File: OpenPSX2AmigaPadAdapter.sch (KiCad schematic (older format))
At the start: 46 parts, among them J1 TO_PSX_PAD, J2 DB9_F, J3 CONN_FTDI, J4 CONN_ICSP, J99 OSHW_LOGO, Q1 BSS138, Q2 BSS138, Q3 BSS138, Q4 BSS138, Q5 BSS138, U1 ATmega328P-AU, U2 TC1185-3.3V, U3 AD5242, Y1 16M, Y2 16M

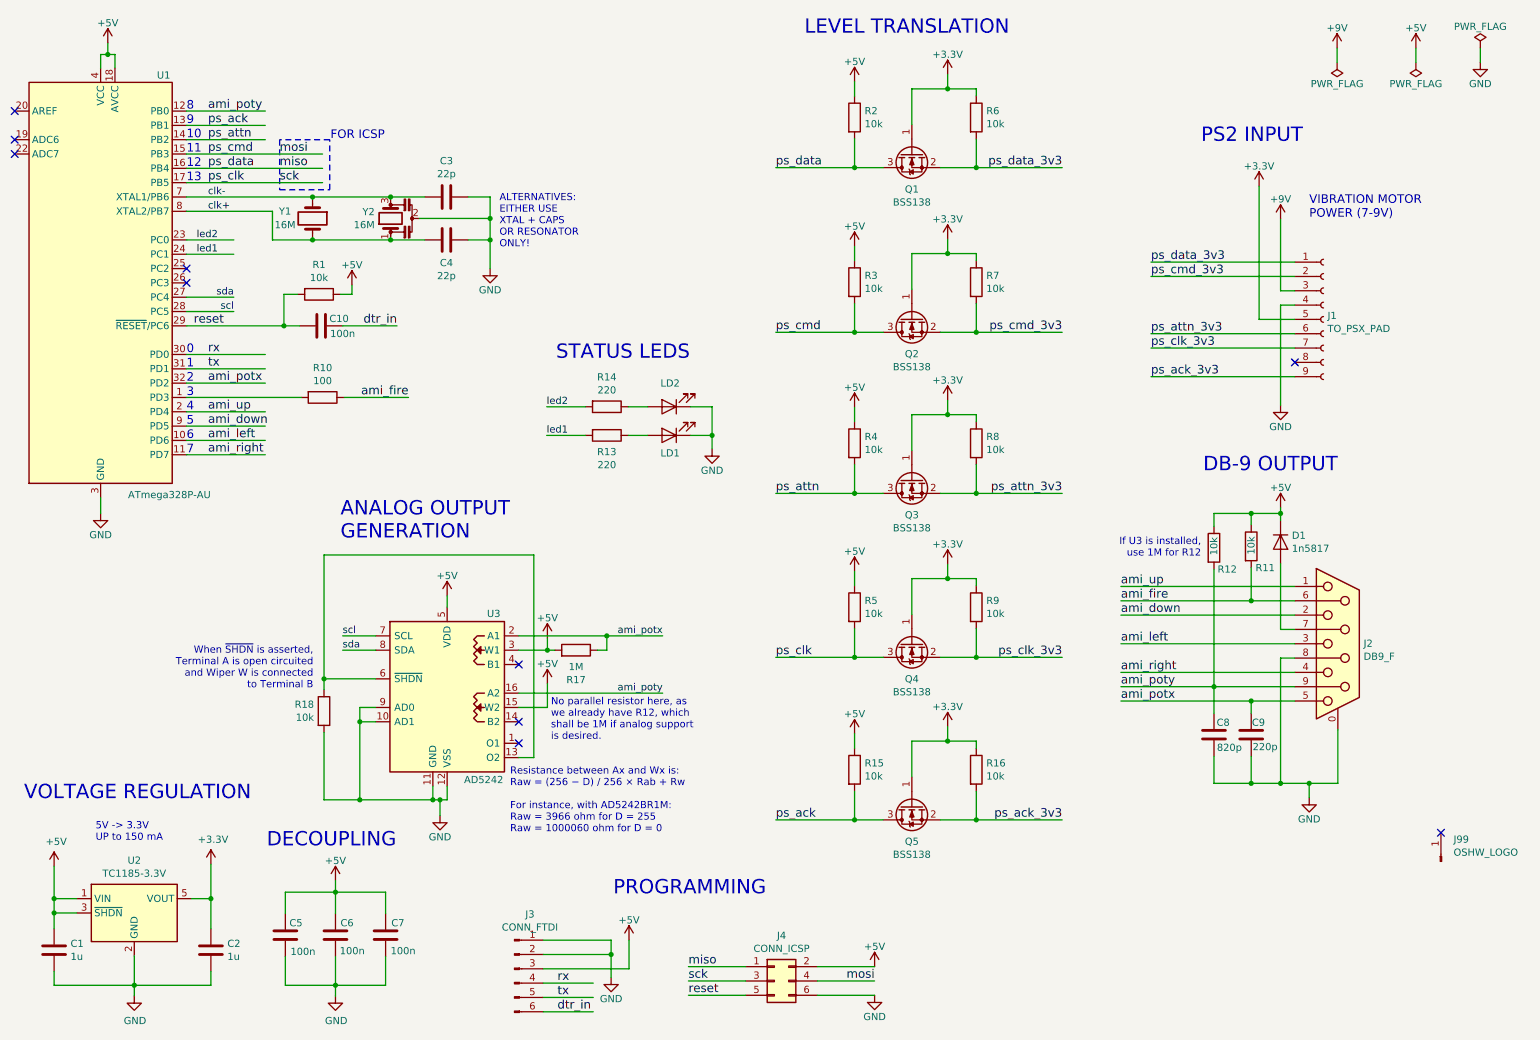
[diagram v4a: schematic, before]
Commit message: Make schematics clearer
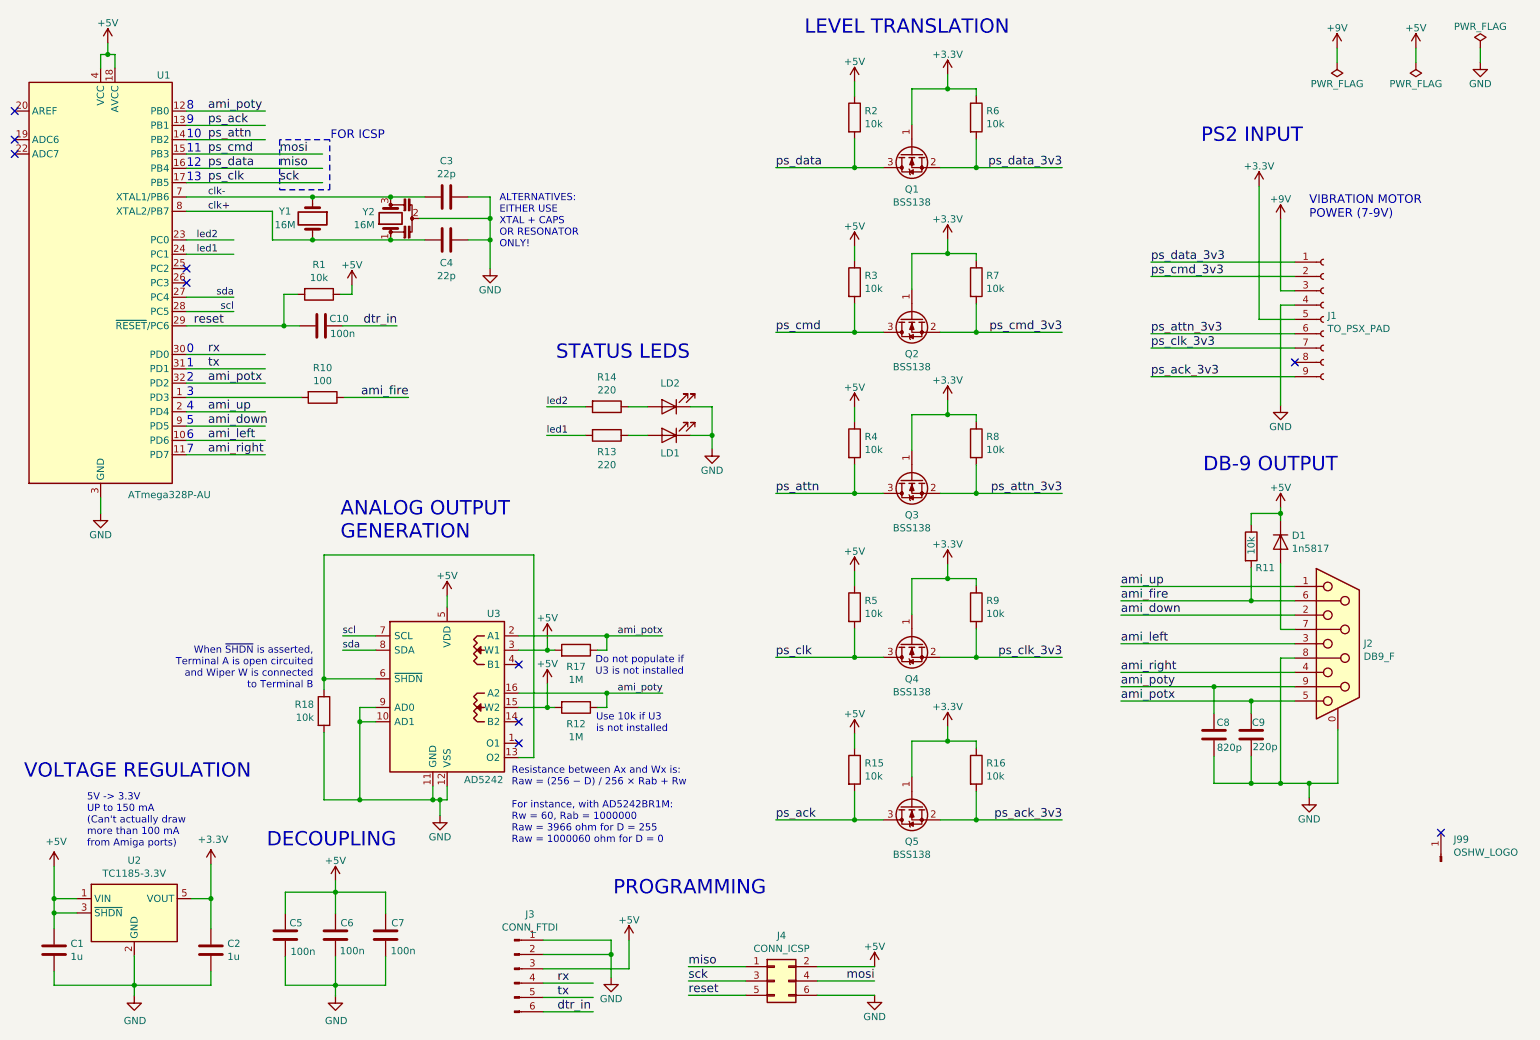
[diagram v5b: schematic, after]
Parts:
- R12: value 10k -> 1M
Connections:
- wire segments 232 -> 233
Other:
- note added: "5V -> 3.3V\nUP to 150 mA\n(Can't actually draw\nmore than 100 mA\nfrom Amiga ports)"
- note added: "Do not populate if\nU3 is not installed"
- note added: "Resistance between Ax and Wx is:\nRaw = (256 − D) / 256 × Rab + Rw\n\nFor instance, with AD5242BR1M:\nRw = 60, Rab = 1000000\nRaw = 3966 ohm for D = 255\nRaw = 1000060 ohm for D = 0"
- note added: "Use 10k if U3\nis not installed"
- note removed: "5V -> 3.3V\nUP to 150 mA"
- note removed: "If U3 is installed,\nuse 1M for R12"
- note removed: "No parallel resistor here, as\nwe already have R12, which\nshall be 1M if analog support\nis desired."
- note removed: "Resistance between Ax and Wx is:\nRaw = (256 − D) / 256 × Rab + Rw\n\nFor instance, with AD5242BR1M:\nRaw = 3966 ohm for D = 255\nRaw = 1000060 ohm for D = 0"
- moved on the sheet: R12
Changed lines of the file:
@@
 	9505 4050 9505 4010
-Wire Wire Line
-	9040 4140 9040 4050
-Wire Wire Line
-	9040 4050 9300 4050
-Connection ~ 9300 4050
 Wire Wire Line
 	9300 4430 9300 4660
@@
 Wire Wire Line
 	9300 4660 8390 4660
-Wire Wire Line
-	9040 4440 9040 5260
 Connection ~ 9040 5260
 Wire Wire Line
@@
 L Device:R R12
 U 1 1 5DAFD7E8
-P 9040 4290
-F 0 "R12" H 9200 4140 50  0000 R CNN
-F 1 "10k" V 9040 4365 50  0000 R CNN
-F 2 "Resistor_SMD:R_0805_2012Metric_Pad1.15x1.40mm_HandSolder" V 8970 4290 50  0001 C CNN
-F 3 "~" H 9040 4290 50  0001 C CNN
-	1    9040 4290
-	1    0    0    -1
+P 4585 5405
+F 0 "R12" V 4700 5405 50  0000 C CNN
+F 1 "1M" V 4791 5405 50  0000 C CNN
+F 2 "Resistor_SMD:R_0805_2012Metric_Pad1.15x1.40mm_HandSolder" V 4515 5405 50  0001 C CNN
+F 3 "~" H 4585 5405 50  0001 C CNN
+	1    4585 5405
+	0    1    1    0
 $EndComp
 $Comp
@@
 AR Path="/5EFED7F9/5F065454" Ref="R?"  Part="1"
 AR Path="/5F065454" Ref="R17"  Part="1"
-F 0 "R17" V 4378 5005 50  0000 C CNN
-F 1 "1M" V 4469 5005 50  0000 C CNN
+F 0 "R17" V 4470 5005 50  0000 C CNN
+F 1 "1M" V 4379 5005 50  0000 C CNN
 F 2 "Resistor_SMD:R_0805_2012Metric_Pad1.15x1.40mm_HandSolder" V 4515 5005 50  0001 C CNN
 F 3 "~" H 4585 5005 50  0001 C CNN
@@
 	1    0    0    -1
 $EndComp
-Text Notes 1230 6345 0    50   ~ 0
-5V -> 3.3V\nUP to 150 mA
+Text Notes 1170 6385 0    50   ~ 0
+5V -> 3.3V\nUP to 150 mA\n(Can't actually draw\nmore than 100 mA\nfrom Amiga ports)
 $Comp
 L Device:C C?
@@
 Wire Wire Line
 	1500 7345 2035 7345
-Text Notes 730  6060 0    100  ~ 0
+Text Notes 730  5910 0    100  ~ 0
 VOLTAGE REGULATION
 Text Notes 2425 6390 0    100  ~ 0
@@
 Wire Wire Line
 	4290 4340 4290 5755
-Text Notes 4125 6285 0    50   ~ 0
-Resistance between Ax and Wx is:\nRaw = (256 − D) / 256 × Rab + Rw\n\nFor instance, with AD5242BR1M:\nRaw = 3966 ohm for D = 255\nRaw = 1000060 ohm for D = 0
+Text Notes 4135 6360 0    50   ~ 0
+Resistance between Ax and Wx is:\nRaw = (256 − D) / 256 × Rab + Rw\n\nFor instance, with AD5242BR1M:\nRw = 60, Rab = 1000000\nRaw = 3966 ohm for D = 255\nRaw = 1000060 ohm for D = 0
 Text Label 2015 1840 0    50   ~ 0
 clk-
@@
 clk+
 Wire Wire Line
-	4185 5305 5190 5305
-Text Notes 4410 5640 0    50   ~ 0
-No parallel resistor here, as\nwe already have R12, which\nshall be 1M if analog support\nis desired.
+	4185 5305 4800 5305
+Text Notes 4725 5585 0    50   ~ 0
+Use 10k if U3\nis not installed
 Text Label 4455 7530 0    60   ~ 0
 dtr_in
-Text Notes 8950 4360 2    50   ~ 0
-If U3 is installed,\nuse 1M for R12
+Wire Wire Line
+	4385 5405 4435 5405
+Connection ~ 4385 5405
+Wire Wire Line
+	4735 5405 4800 5405
+Wire Wire Line
+	4800 5405 4800 5305
+Connection ~ 4800 5305
+Wire Wire Line
+	4800 5305 5190 5305
+Text Notes 4720 5185 0    50   ~ 0
+Do not populate if\nU3 is not installed
 $EndSCHEMATC
